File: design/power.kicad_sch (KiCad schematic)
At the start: 56 parts, among them J1 POWER, U1 LM3880MF-1AA, U2 NCP59744MN1, U3 NCP59744MN1, U4 NCP59744MN1, U5 NCP59744MN1

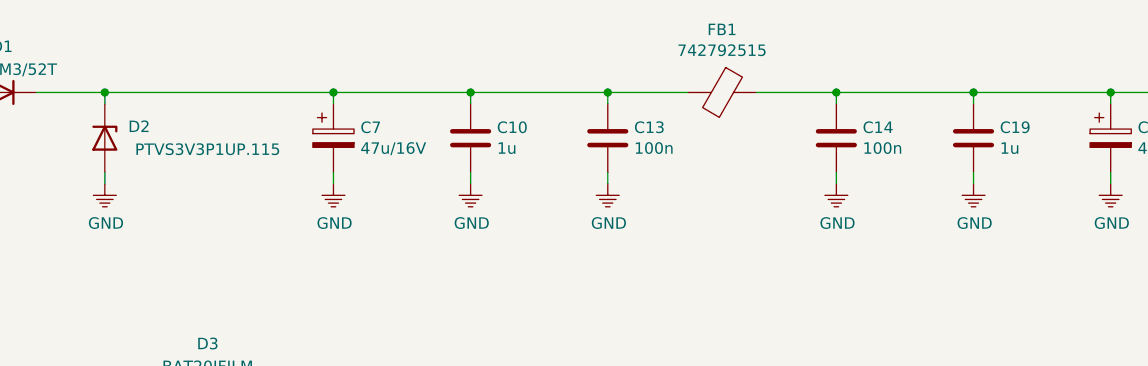
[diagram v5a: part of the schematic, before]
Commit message: Added power polygons
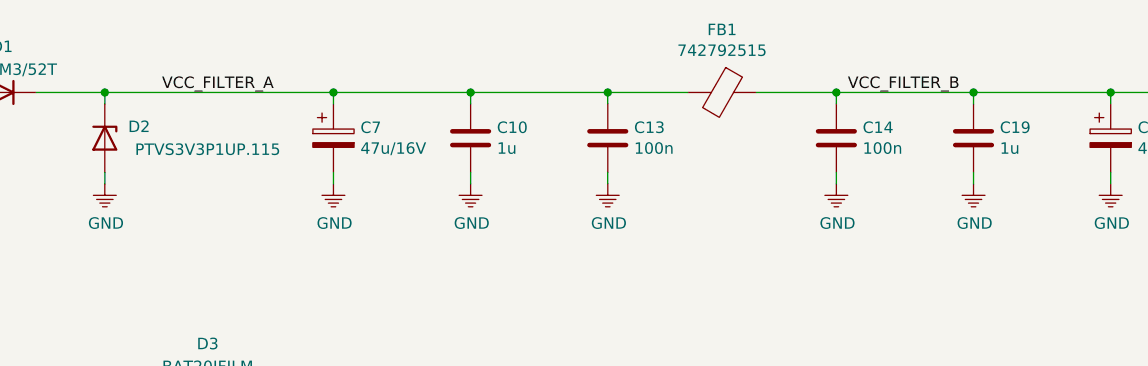
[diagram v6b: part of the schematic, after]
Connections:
- net VCC_FILTER_B: now reaches C14.1, C19.1, C22.1, FB1.1, L1.1
- net VCC_FILTER_A: now reaches C10.1, C13.1, C7.1, D1.1 (K), D2.1 (K), FB1.2
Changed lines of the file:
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@@
-(kicad_sch (version 20200506) (host eeschema "5.99.0-unknown-1f9723c~101~ubuntu18.04.1")
+(kicad_sch (version 20200506) (host eeschema "5.99.0-unknown-302646c~101~ubuntu18.04.1")
   (page "A4")
   (title_block
@@
     (company "Jan Vykydal")
   )
-  (junction (at 128.27 74.93))
+  (junction (at 176.53 123.19))
+  (junction (at 220.98 29.21))
+  (junction (at 95.25 177.8))
+  (junction (at 39.37 175.26))
+  (junction (at 176.53 73.66))
+  (junction (at 128.27 123.19))
+  (junction (at 165.1 29.21))
+  (junction (at 231.14 73.66))
+  (junction (at 220.98 73.66))
+  (junction (at 73.66 123.19))
+  (junction (at 83.82 29.21))
+  (junction (at 86.36 162.56))
+  (junction (at 196.85 73.66))
+  (junction (at 251.46 29.21))
+  (junction (at 220.98 83.82))
+  (junction (at 116.84 74.93))
+  (junction (at 106.68 133.35))
+  (junction (at 57.15 162.56))
+  (junction (at 187.96 123.19))
+  (junction (at 236.22 29.21))
+  (junction (at 180.34 29.21))
+  (junction (at 77.47 172.72))
+  (junction (at 195.58 29.21))
+  (junction (at 139.7 29.21))
+  (junction (at 196.85 123.19))
+  (junction (at 82.55 123.19))
+  (junction (at 109.22 29.21))
+  (junction (at 62.23 123.19))
+  (junction (at 86.36 175.26))
+  (junction (at 52.07 74.93))
+  (junction (at 77.47 162.56))
+  (junction (at 187.96 73.66))
+  (junction (at 166.37 73.66))
+  (junction (at 231.14 123.19))
+  (junction (at 220.98 123.19))
+  (junction (at 242.57 73.66))
+  (junction (at 106.68 85.09))
+  (junction (at 62.23 74.93))
+  (junction (at 106.68 74.93))
+  (junction (at 82.55 74.93))
+  (junction (at 166.37 123.19))
+  (junction (at 53.34 29.21))
+  (junction (at 116.84 123.19))
+  (junction (at 53.34 36.83))
+  (junction (at 124.46 29.21))
   (junction (at 242.57 123.19))
-  (junction (at 82.55 74.93))
-  (junction (at 124.46 29.21))
-  (junction (at 236.22 29.21))
-  (junction (at 139.7 29.21))
-  (junction (at 187.96 73.66))
-  (junction (at 39.37 175.26))
-  (junction (at 128.27 123.19))
-  (junction (at 220.98 123.19))
-  (junction (at 187.96 123.19))
-  (junction (at 196.85 73.66))
-  (junction (at 165.1 29.21))
-  (junction (at 82.55 123.19))
-  (junction (at 220.98 29.21))
-  (junction (at 62.23 74.93))
-  (junction (at 86.36 162.56))
-  (junction (at 196.85 123.19))
-  (junction (at 166.37 73.66))
-  (junction (at 60.96 29.21))
+  (junction (at 220.98 133.35))
   (junction (at 73.66 74.93))
   (junction (at 106.68 123.19))
-  (junction (at 53.34 36.83))
-  (junction (at 86.36 175.26))
-  (junction (at 106.68 74.93))
-  (junction (at 95.25 177.8))
-  (junction (at 77.47 162.56))
+  (junction (at 60.96 29.21))
   (junction (at 52.07 123.19))
-  (junction (at 180.34 29.21))
-  (junction (at 220.98 83.82))
-  (junction (at 242.57 73.66))
-  (junction (at 251.46 29.21))
-  (junction (at 116.84 74.93))
-  (junction (at 116.84 123.19))
-  (junction (at 52.07 74.93))
-  (junction (at 73.66 123.19))
-  (junction (at 176.53 123.19))
-  (junction (at 83.82 29.21))
-  (junction (at 220.98 133.35))
-  (junction (at 195.58 29.21))
-  (junction (at 57.15 162.56))
-  (junction (at 166.37 123.19))
-  (junction (at 106.68 85.09))
-  (junction (at 176.53 73.66))
-  (junction (at 77.47 172.72))
-  (junction (at 62.23 123.19))
-  (junction (at 220.98 73.66))
-  (junction (at 109.22 29.21))
-  (junction (at 231.14 123.19))
-  (junction (at 53.34 29.21))
-  (junction (at 231.14 73.66))
-  (junction (at 106.68 133.35))
+  (junction (at 128.27 74.93))
+  (no_connect (at 85.09 135.89))
+  (no_connect (at 199.39 135.89))
   (no_connect (at 199.39 86.36))
-  (no_connect (at 199.39 135.89))
-  (no_connect (at 85.09 135.89))
   (no_connect (at 85.09 87.63))
   (wire (pts (xy 39.37 161.29) (xy 39.37 163.83)))
@@
     (effects (font (size 1.27 1.27)) (justify right bottom))
   )
+  (label "VCC_FILTER_A" (at 90.17 29.21 0)
+    (effects (font (size 1.27 1.27)) (justify left bottom))
+  )
   (label "EN_1V0" (at 91.44 93.98 180)
     (effects (font (size 1.27 1.27)) (justify right bottom))
@@
     (effects (font (size 1.27 1.27)) (justify right bottom))
   )
+  (label "VCC_FILTER_B" (at 166.37 29.21 0)
+    (effects (font (size 1.27 1.27)) (justify left bottom))
+  )
   (label "EN_1V8" (at 205.74 92.71 180)
